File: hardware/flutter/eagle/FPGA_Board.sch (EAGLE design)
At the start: 38 parts, among them IC1 AT45DB161D-SU, U2 XC3S50AVQ100

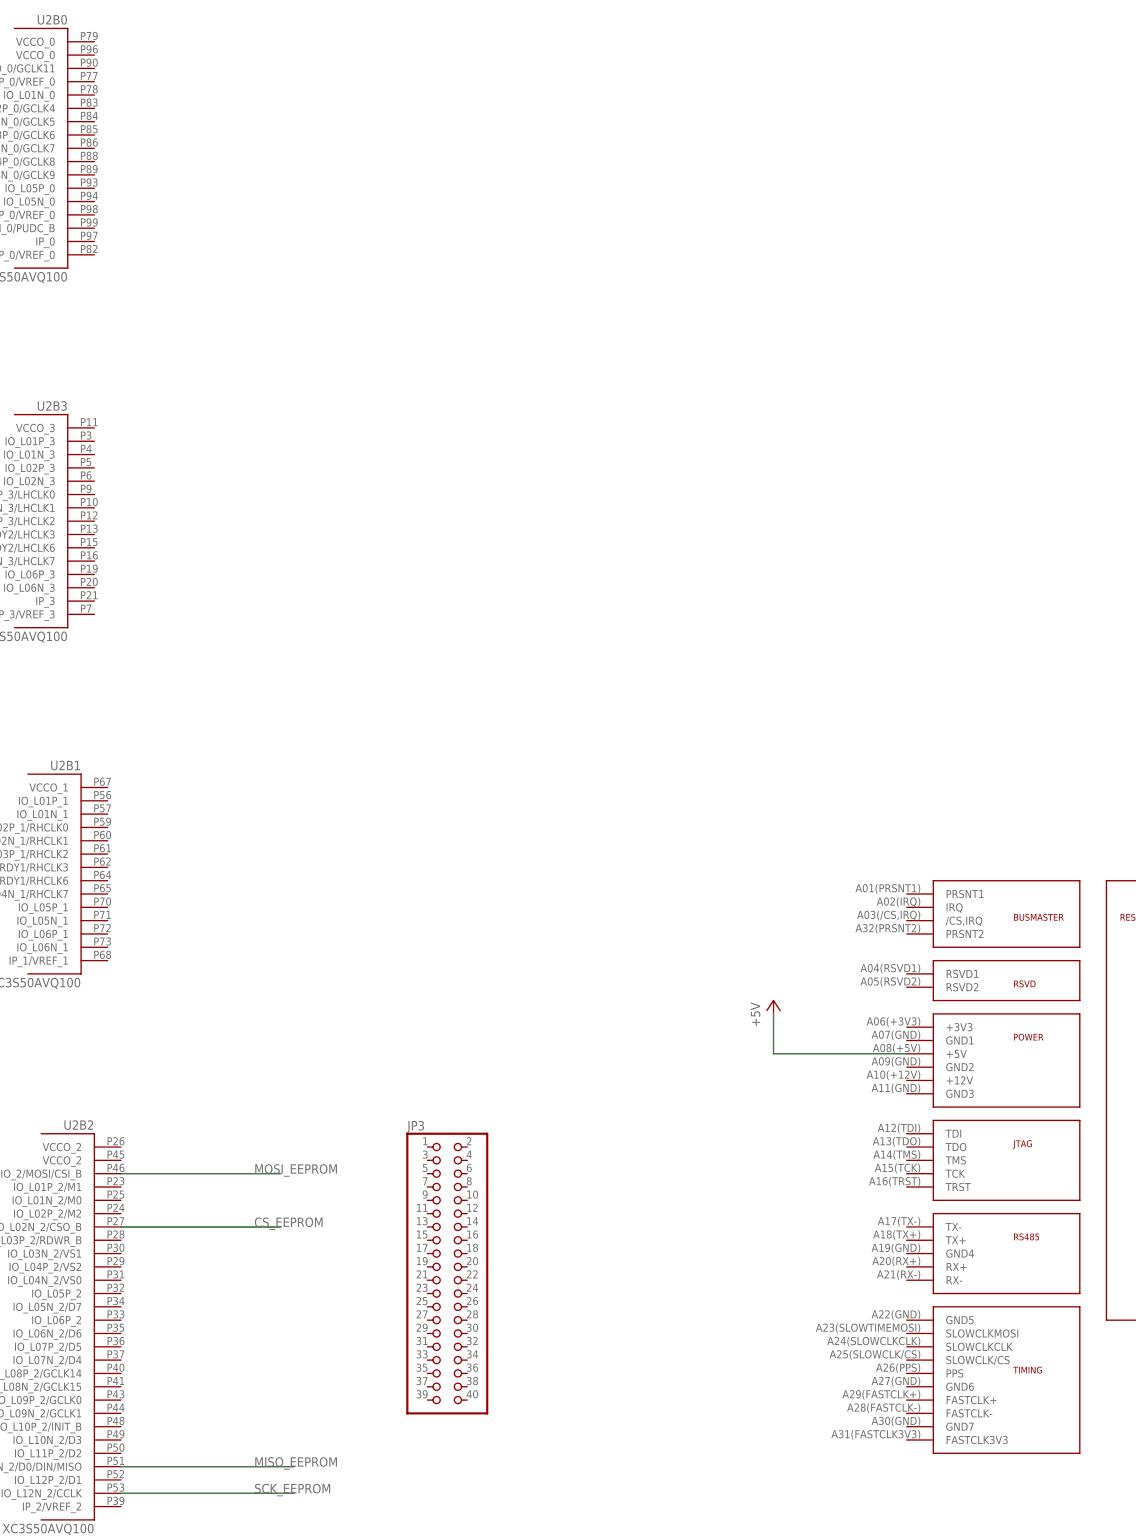
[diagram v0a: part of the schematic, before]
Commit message: connected FPGA to friendship connector
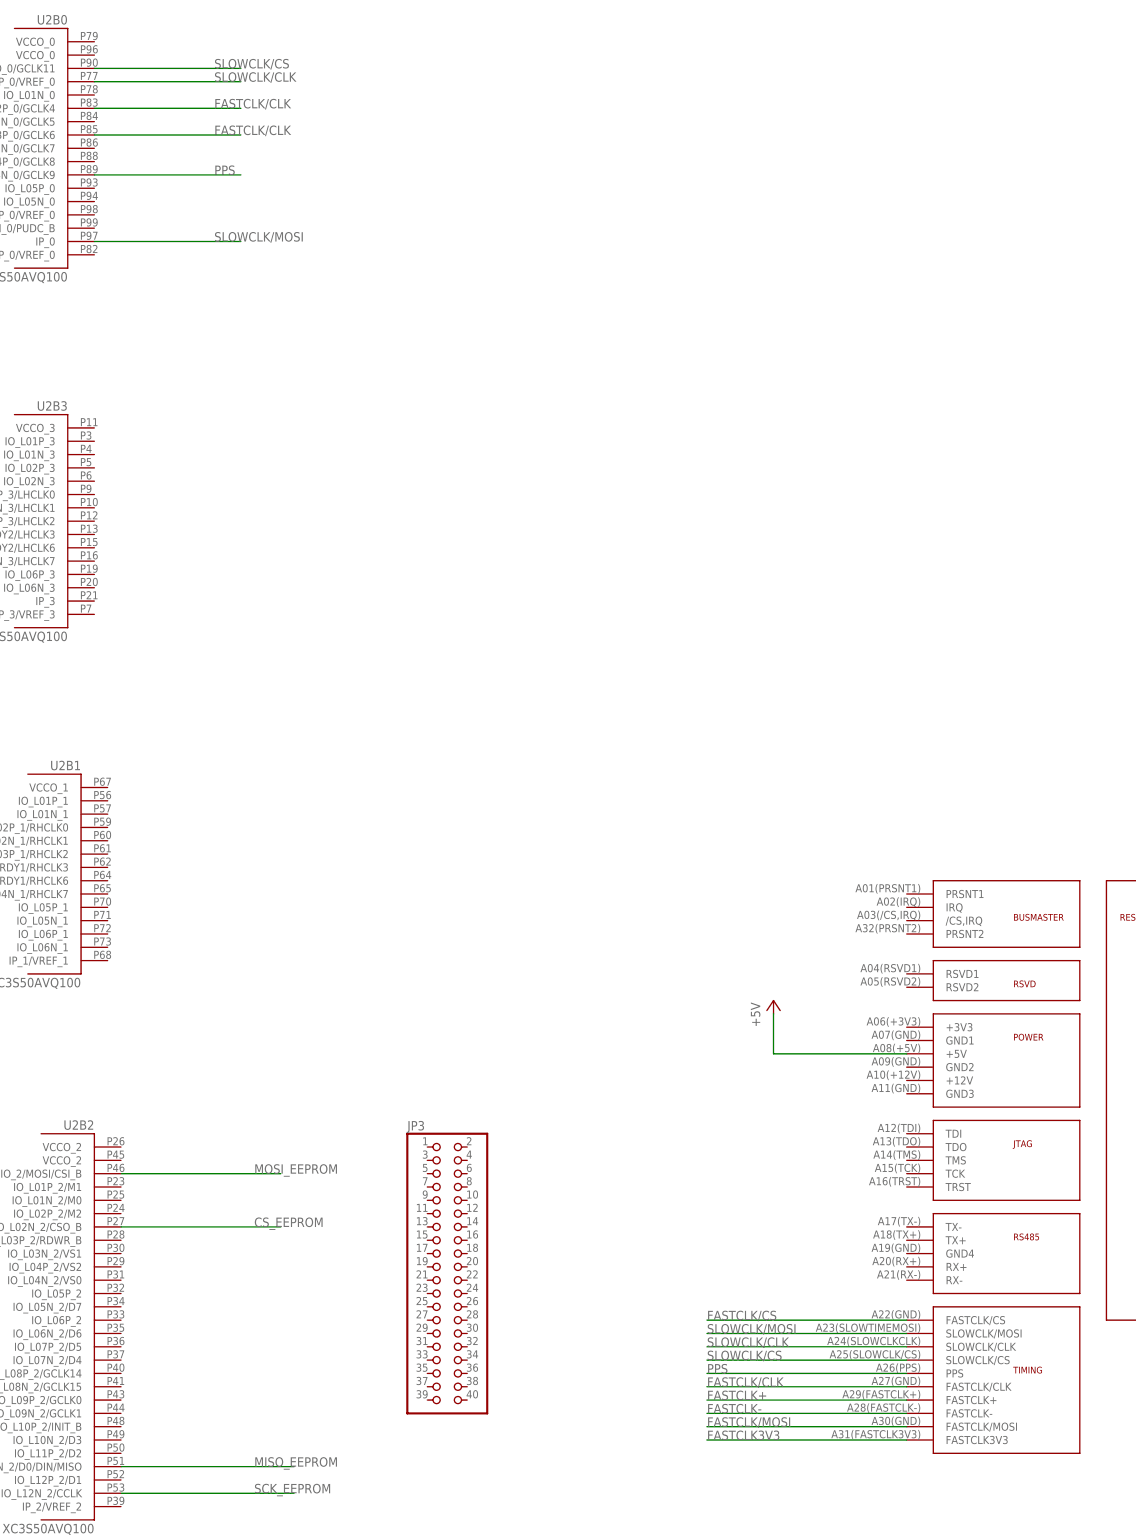
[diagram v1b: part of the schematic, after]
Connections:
- new net FASTCLK+: U$4.FASTCLK+
- new net FASTCLK-: U$4.FASTCLK-
- new net FASTCLK/CLK: U$4.FASTCLK/CLK, U2B0.IO_L02P_0/GCLK4, U2B0.IO_L03P_0/GCLK6
- new net FASTCLK/CS: U$4.FASTCLK/CS
- new net FASTCLK/MOSI: U$4.FASTCLK/MOSI
- new net FASTCLK3V3: U$4.FASTCLK3V3
- new net PPS: U$4.PPS, U2B0.IO_L04N_0/GCLK9
- new net SLOWCLK/CLK: U$4.SLOWCLK/CLK, U2B0.IO_L01P_0/VREF_0
- new net SLOWCLK/CS: U$4.SLOWCLK/CS, U2B0.IO_0/GCLK11
- new net SLOWCLK/MOSI: U$4.SLOWCLK/MOSI, U2B0.IP_0
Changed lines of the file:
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@@
+</segment>
+</net>
+<net name="FASTCLK/CS" class="0">
+<segment>
+<pinref part="U$4" gate="G$1" pin="FASTCLK/CS"/>
+<wire x1="307.34" y1="215.9" x2="269.24" y2="215.9" width="0.1524" layer="91"/>
+<label x="269.24" y="215.9" size="1.778" layer="95"/>
+</segment>
+</net>
+<net name="SLOWCLK/MOSI" class="0">
+<segment>
+<pinref part="U$4" gate="G$1" pin="SLOWCLK/MOSI"/>
+<wire x1="307.34" y1="213.36" x2="269.24" y2="213.36" width="0.1524" layer="91"/>
+<label x="269.24" y="213.36" size="1.778" layer="95"/>
+</segment>
+<segment>
+<pinref part="U2" gate="B0" pin="IP_0"/>
+<wire x1="152.4" y1="421.64" x2="180.34" y2="421.64" width="0.1524" layer="91"/>
+<label x="175.26" y="421.64" size="1.778" layer="95"/>
+</segment>
+</net>
+<net name="SLOWCLK/CLK" class="0">
+<segment>
+<pinref part="U$4" gate="G$1" pin="SLOWCLK/CLK"/>
+<wire x1="307.34" y1="210.82" x2="269.24" y2="210.82" width="0.1524" layer="91"/>
+<label x="269.24" y="210.82" size="1.778" layer="95"/>
+</segment>
+<segment>
+<pinref part="U2" gate="B0" pin="IO_L01P_0/VREF_0"/>
+<wire x1="152.4" y1="452.12" x2="180.34" y2="452.12" width="0.1524" layer="91"/>
+<label x="175.26" y="452.12" size="1.778" layer="95"/>
+</segment>
+</net>
+<net name="SLOWCLK/CS" class="0">
+<segment>
+<pinref part="U$4" gate="G$1" pin="SLOWCLK/CS"/>
+<wire x1="307.34" y1="208.28" x2="269.24" y2="208.28" width="0.1524" layer="91"/>
+<label x="269.24" y="208.28" size="1.778" layer="95"/>
+</segment>
+<segment>
+<pinref part="U2" gate="B0" pin="IO_0/GCLK11"/>
+<wire x1="152.4" y1="454.66" x2="180.34" y2="454.66" width="0.1524" layer="91"/>
+<label x="175.26" y="454.66" size="1.778" layer="95"/>
+</segment>
+</net>
+<net name="PPS" class="0">
+<segment>
+<pinref part="U$4" gate="G$1" pin="PPS"/>
+<wire x1="307.34" y1="205.74" x2="269.24" y2="205.74" width="0.1524" layer="91"/>
+<label x="269.24" y="205.74" size="1.778" layer="95"/>
+</segment>
+<segment>
+<pinref part="U2" gate="B0" pin="IO_L04N_0/GCLK9"/>
+<wire x1="152.4" y1="434.34" x2="180.34" y2="434.34" width="0.1524" layer="91"/>
+<label x="175.26" y="434.34" size="1.778" layer="95"/>
+</segment>
+</net>
+<net name="FASTCLK/CLK" class="0">
+<segment>
+<pinref part="U$4" gate="G$1" pin="FASTCLK/CLK"/>
+<wire x1="307.34" y1="203.2" x2="269.24" y2="203.2" width="0.1524" layer="91"/>
+<label x="269.24" y="203.2" size="1.778" layer="95"/>
+</segment>
+<segment>
+<pinref part="U2" gate="B0" pin="IO_L02P_0/GCLK4"/>
+<wire x1="152.4" y1="447.04" x2="180.34" y2="447.04" width="0.1524" layer="91"/>
+<label x="175.26" y="447.04" size="1.778" layer="95"/>
+</segment>
+<segment>
+<pinref part="U2" gate="B0" pin="IO_L03P_0/GCLK6"/>
+<wire x1="152.4" y1="441.96" x2="180.34" y2="441.96" width="0.1524" layer="91"/>
+<label x="175.26" y="441.96" size="1.778" layer="95"/>
+</segment>
+</net>
+<net name="FASTCLK+" class="0">
+<segment>
+<pinref part="U$4" gate="G$1" pin="FASTCLK+"/>
+<wire x1="307.34" y1="200.66" x2="269.24" y2="200.66" width="0.1524" layer="91"/>
+<label x="269.24" y="200.66" size="1.778" layer="95"/>
+</segment>
+</net>
+<net name="FASTCLK-" class="0">
+<segment>
+<pinref part="U$4" gate="G$1" pin="FASTCLK-"/>
+<wire x1="307.34" y1="198.12" x2="269.24" y2="198.12" width="0.1524" layer="91"/>
+<label x="269.24" y="198.12" size="1.778" layer="95"/>
+</segment>
+</net>
+<net name="FASTCLK/MOSI" class="0">
+<segment>
+<pinref part="U$4" gate="G$1" pin="FASTCLK/MOSI"/>
+<wire x1="307.34" y1="195.58" x2="269.24" y2="195.58" width="0.1524" layer="91"/>
+<label x="269.24" y="195.58" size="1.778" layer="95"/>
+</segment>
+</net>
+<net name="FASTCLK3V3" class="0">
+<segment>
+<pinref part="U$4" gate="G$1" pin="FASTCLK3V3"/>
+<wire x1="307.34" y1="193.04" x2="269.24" y2="193.04" width="0.1524" layer="91"/>
+<label x="269.24" y="193.04" size="1.778" layer="95"/>
 </segment>
 </net>
